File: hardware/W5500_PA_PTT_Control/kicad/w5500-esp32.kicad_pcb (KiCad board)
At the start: 4 copper layers, 72 x 115 mm, 26 parts, among them J1 ESP32_DevKitC_Socket_40P_25.4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, J2 DC_IN_13V8, J5 Power, J6 PTT_ON, Q1 2SC1815, Q3 2SC1815, Q5 2SJ334, U1 TA48033S, U2 L7805

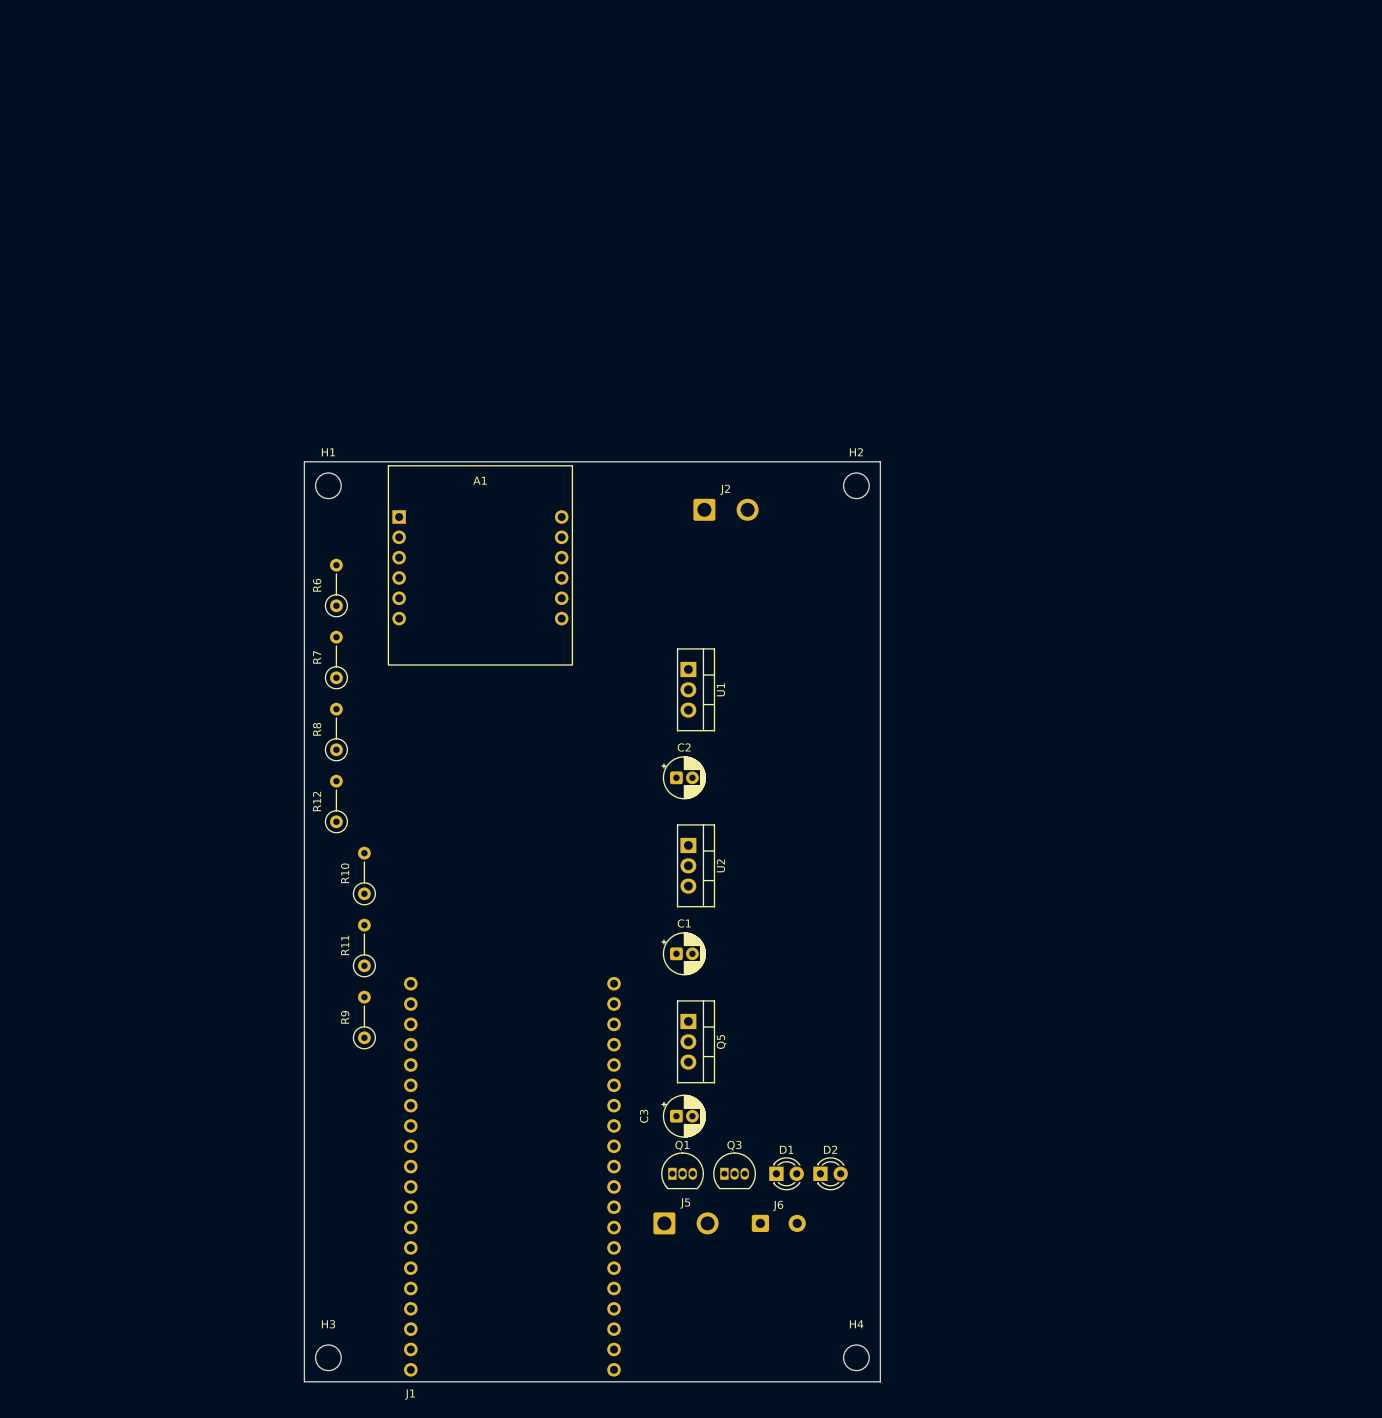
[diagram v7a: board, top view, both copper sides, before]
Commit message: W5500制御基板: 放熱器の枠を部品位置に合わせ取付穴位置を反映
- 放熱器の枠(Dwgs.User)が旧位置に残っていたのを修正し、TO-220のタブ裏にそろえて中央の足に穴の中心を合わせた
- 放熱器の取付穴(下端から18mm・幅の中央)の印を追加
- 仕様書(日英)に取付穴位置と部品の取付高さを追記、Word/PDFを再生成

Co-Authored-By: Claude Opus 5.5 <noreply@anthropic.com>
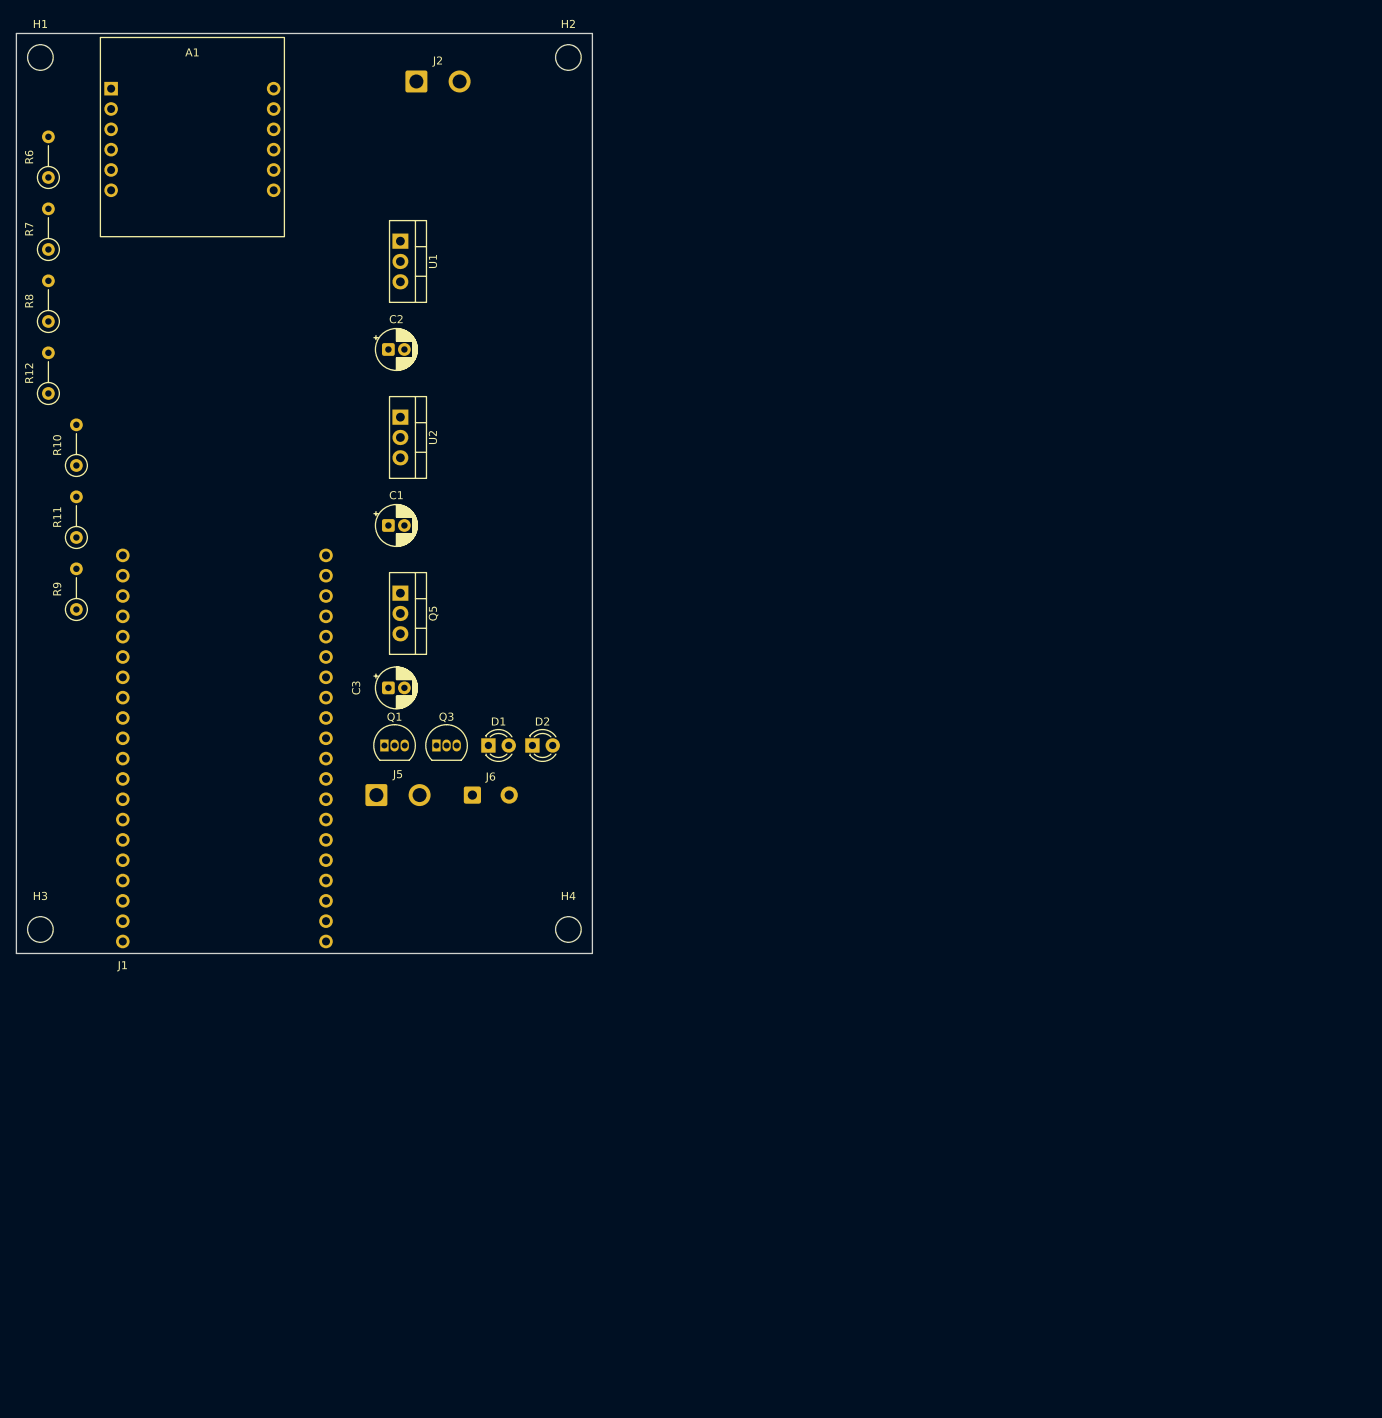
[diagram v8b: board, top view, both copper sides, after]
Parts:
- moved A1 64.5 mm to (75.8, 53.4)
- moved C1 64.5 mm to (110.5, 108.0)
- moved C2 64.5 mm to (110.5, 86.0)
- moved C3 64.5 mm to (110.5, 128.3)
- moved J1 64.5 mm to (77.3, 111.7)
- moved Q5 64.5 mm to (112.0, 116.4)
- moved R10 64.5 mm to (71.5, 100.5)
- moved R11 64.5 mm to (71.5, 109.5)
- moved R12 64.5 mm to (68.0, 91.5)
- moved R6 64.5 mm to (68.0, 64.5)
- moved R7 64.5 mm to (68.0, 73.5)
- moved R8 64.5 mm to (68.0, 82.5)
- moved R9 64.5 mm to (71.5, 118.5)
- moved U2 64.5 mm to (112.0, 94.4)
- moved D1 64.5 mm to (123.0, 135.5)
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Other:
- board text added: "放熱器 Q5 20x20 (M3穴 高さ18)"
- board text added: "放熱器 U1 20x20 (M3穴 高さ18)"
- board text added: "放熱器 U2 20x20 (M3穴 高さ18)"
- board text removed: "放熱器 Q5 20x20"
- board text removed: "放熱器 U1 20x20"
- board text removed: "放熱器 U2 20x20"
